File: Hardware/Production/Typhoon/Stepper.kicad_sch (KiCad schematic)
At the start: 14 parts, among them IC1 TMC2209-LA, J3 Motor Breakout

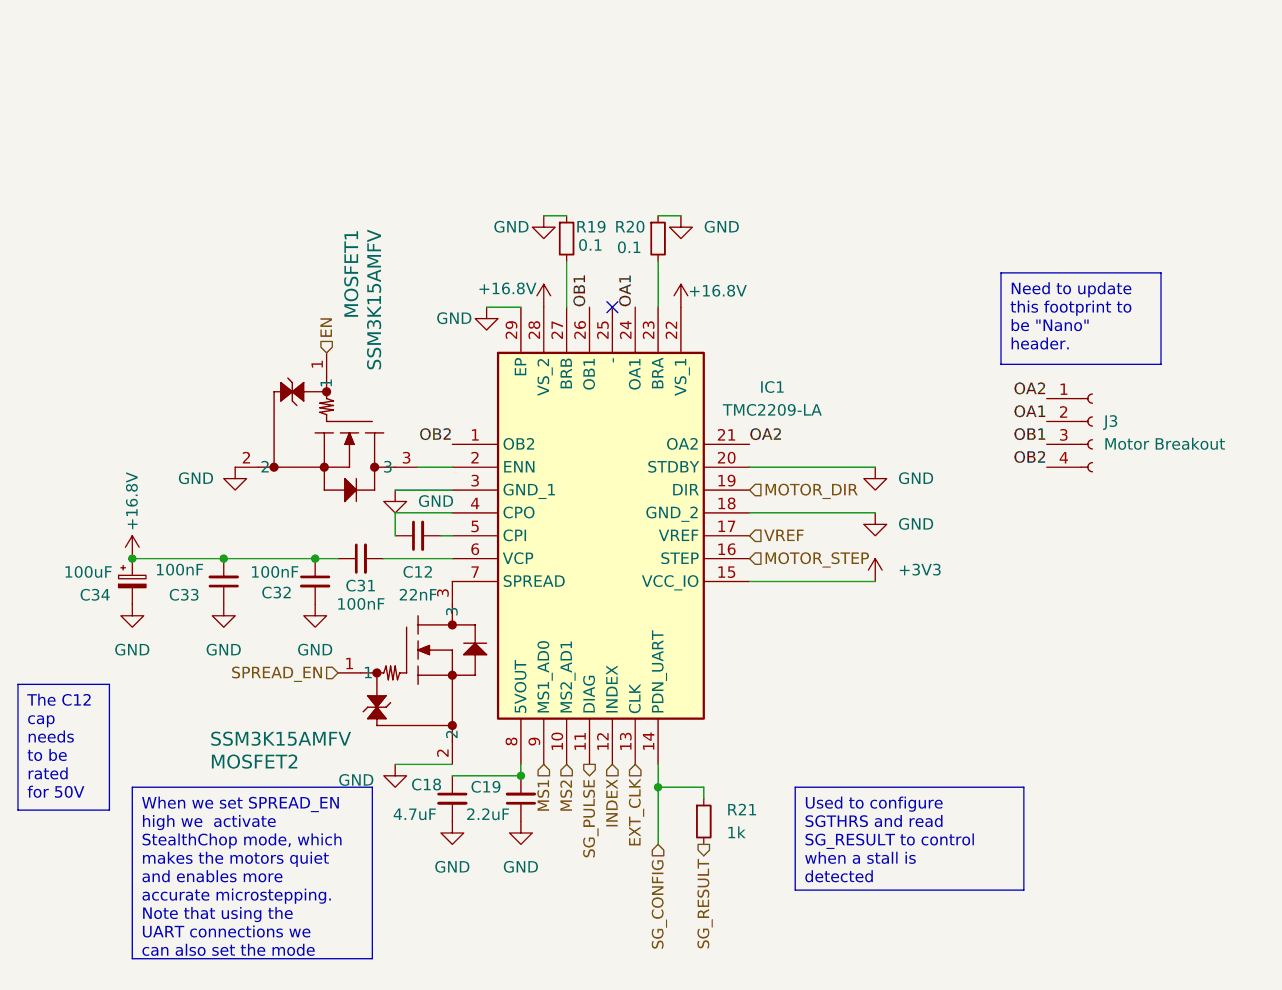
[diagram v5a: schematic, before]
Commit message: Small fixes to some footprints and used a different model for NMOS transistors
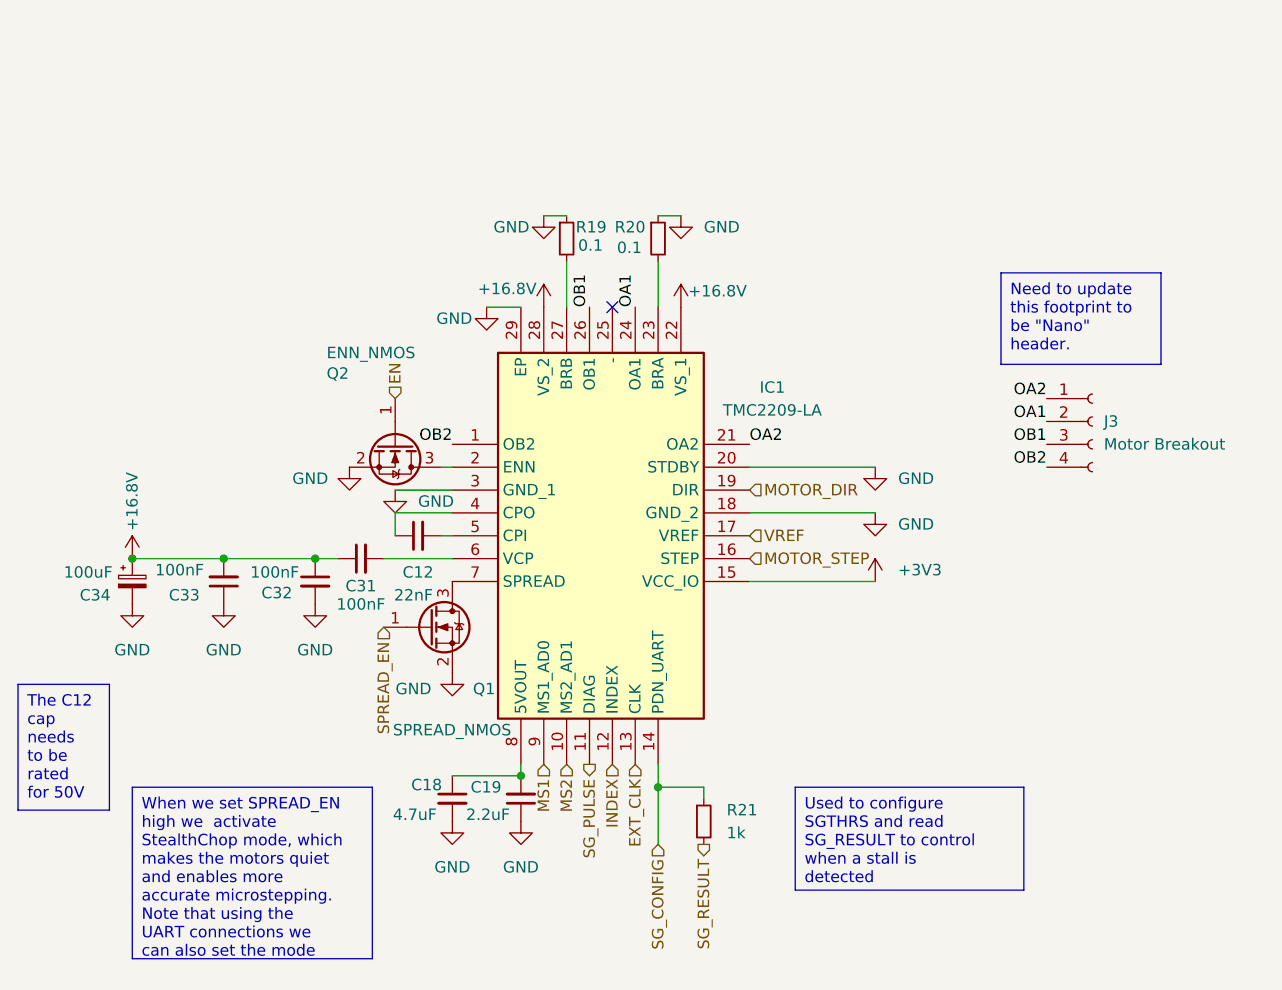
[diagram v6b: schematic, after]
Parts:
- removed MOSFET1, MOSFET2: SSM3K15AMFV, VESM_TOS, symbol SSM3K15AMFV:SSM3K15AMFV
- added Q1: SPREAD_NMOS, iclr:SOT-723, symbol Device:Q_NMOS_GSD
- added Q2: ENN_NMOS, iclr:SOT-723, symbol Device:Q_NMOS_GSD
- J3: footprint Connector_Molex:Molex_Nano-Fit_105313-xx04_1x04_P2.50mm_Horizontal -> iclr:Molex_Nano-Fit_105313-xx04_1x04_P2.50mm_Horizontal
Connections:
- net EN: now also Q2.1 (G)
- net GND: now also Q1.2 (S), Q2.2 (S)
- net SPREAD_EN: now also Q1.1 (G)
- net at IC1.7 (SPREAD): now also Q1.3 (D)
- net at IC1.2 (ENN): now also Q2.3 (D)
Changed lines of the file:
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@@
 	(wire
 		(pts
-			(xy 106.68 133.35) (xy 100.33 133.35)
+			(xy 134.62 135.89) (xy 134.62 137.16)
 		)
 		(stroke
@@
 	(wire
 		(pts
-			(xy 134.62 135.89) (xy 134.62 137.16)
+			(xy 106.68 134.62) (xy 114.3 134.62)
 		)
 		(stroke
@@
 	(wire
 		(pts
-			(xy 106.68 134.62) (xy 114.3 134.62)
-		)
-		(stroke
-			(width 0)
-			(type default)
-		)
-	)
-	(wire
-		(pts
-			(xy 102.87 100.33) (xy 106.68 100.33)
+			(xy 105.41 100.33) (xy 106.68 100.33)
 		)
 		(stroke
@@
 	(hierarchical_label "EN"
 		(shape input)
-		(at 92.71 87.63 90)
+		(at 100.33 92.71 90)
 		(fields_autoplaced yes)
 		(effects
@@
 	(hierarchical_label "SPREAD_EN"
 		(shape input)
-		(at 93.98 123.19 180)
+		(at 99.06 118.11 270)
 		(fields_autoplaced yes)
 		(effects
@@
 	(symbol
 		(lib_id "power:GND")
-		(at 100.33 133.35 0)
+		(at 106.68 123.19 0)
 		(unit 1)
 		(exclude_from_sim no)
@@
 		(dnp no)
 		(property "Reference" "#PWR068"
-			(at 100.33 139.7 0)
+			(at 106.68 129.54 0)
 			(effects
 				(font
@@
 		)
 		(property "Value" "GND"
-			(at 96.012 135.128 0)
+			(at 102.362 124.968 0)
 			(effects
 				(font
@@
 		)
 		(property "Footprint" ""
-			(at 100.33 133.35 0)
+			(at 106.68 123.19 0)
 			(effects
 				(font
@@
 		)
 		(property "Datasheet" ""
-			(at 100.33 133.35 0)
+			(at 106.68 123.19 0)
 			(effects
 				(font
@@
 		)
 		(property "Description" "Power symbol creates a global label with name \"GND\" , ground"
-			(at 100.33 133.35 0)
+			(at 106.68 123.19 0)
 			(effects
 				(font
@@
 				(path "/7db990e4-92e1-4f99-b4d2-435bbec1ba83/8de86a23-669c-43a7-bbab-df851b7a13ef"
 					(reference "C18")
+					(unit 1)
+				)
+			)
+		)
+	)
+	(symbol
+		(lib_id "Device:Q_NMOS_GSD")
+		(at 100.33 97.79 270)
+		(unit 1)
+		(exclude_from_sim no)
+		(in_bom yes)
+		(on_board yes)
+		(dnp no)
+		(property "Reference" "Q2"
+			(at 92.71 89.916 90)
+			(effects
+				(font
+					(size 1.27 1.27)
+				)
+				(justify left)
+			)
+		)
+		(property "Value" "ENN_NMOS"
+			(at 92.71 87.63 90)
+			(effects
+				(font
+					(size 1.27 1.27)
+				)
+				(justify left)
+			)
+		)
+		(property "Footprint" "iclr:SOT-723"
+			(at 102.87 102.87 0)
+			(effects
+				(font
+					(size 1.27 1.27)
+				)
+				(hide yes)
+			)
+		)
+		(property "Datasheet" "~"
+			(at 100.33 97.79 0)
+			(effects
+				(font
+					(size 1.27 1.27)
+				)
+				(hide yes)
+			)
+		)
+		(property "Description" "N-MOSFET transistor, gate/source/drain"
+			(at 100.33 97.79 0)
+			(effects
+				(font
+					(size 1.27 1.27)
+				)
+				(hide yes)
+			)
+		)
+		(pin "2"
+		)
+		(pin "3"
+		)
+		(pin "1"
+		)
+		(instances
+			(project "Typhoon"
+				(path "/7db990e4-92e1-4f99-b4d2-435bbec1ba83/8de86a23-669c-43a7-bbab-df851b7a13ef"
+					(reference "Q2")
 					(unit 1)
 				)
@@
 		(lib_name "GND_2")
 		(lib_id "power:GND")
-		(at 82.55 100.33 0)
+		(at 95.25 100.33 0)
 		(unit 1)
 		(exclude_from_sim no)
@@
 		(dnp no)
 		(property "Reference" "#PWR016"
-			(at 82.55 106.68 0)
+			(at 95.25 106.68 0)
 			(effects
 				(font
@@
 		)
 		(property "Value" "GND"
-			(at 76.2 101.6 0)
+			(at 88.9 101.6 0)
 			(effects
 				(font
@@
 		)
 		(property "Footprint" ""
-			(at 82.55 100.33 0)
+			(at 95.25 100.33 0)
 			(effects
 				(font
@@
 		)
 		(property "Datasheet" ""
-			(at 82.55 100.33 0)
+			(at 95.25 100.33 0)
 			(effects
 				(font
@@
 		)
 		(property "Description" "Power symbol creates a global label with name \"GND\" , ground"
-			(at 82.55 100.33 0)
+			(at 95.25 100.33 0)
 			(effects
 				(font
@@
 	)
 	(symbol
-		(lib_id "SSM3K15AMFV:SSM3K15AMFV")
-		(at 96.52 115.57 0)
-		(unit 1)
-		(exclude_from_sim no)
-		(in_bom yes)
-		(on_board yes)
-		(dnp no)
-		(property "Reference" "MOSFET2"
-			(at 79.756 133.096 0)
-			(effects
-				(font
-					(size 1.524 1.524)
-				)
-				(justify left)
-			)
-		)
-		(property "Value" "SSM3K15AMFV"
-			(at 79.756 130.556 0)
-			(effects
-				(font
-					(size 1.524 1.524)
-				)
-				(justify left)
-			)
-		)
-		(property "Footprint" "VESM_TOS"
-			(at 96.52 115.57 0)
-			(effects
-				(font
-					(size 1.27 1.27)
-					(italic yes)
-				)
-				(hide yes)
-			)
-		)
-		(property "Datasheet" "SSM3K15AMFV"
-			(at 96.52 115.57 0)
-			(effects
-				(font
-					(size 1.27 1.27)
-					(italic yes)
-				)
-				(hide yes)
-			)
-		)
-		(property "Description" ""
-			(at 96.52 115.57 0)
-			(effects
-				(font
-					(size 1.27 1.27)
-				)
-				(hide yes)
-			)
-		)
-		(pin "2"
-		)
-		(pin "1"
-		)
-		(pin "3"
-		)
-		(instances
-			(project "Typhoon"
-				(path "/7db990e4-92e1-4f99-b4d2-435bbec1ba83/8de86a23-669c-43a7-bbab-df851b7a13ef"
-					(reference "MOSFET2")
-					(unit 1)
-				)
-			)
-		)
-	)
-	(symbol
 		(lib_id "Device:C_Polarized_Small")
 		(at 71.12 113.03 0)
@@
 			)
 		)
-		(property "Footprint" "Connector_Molex:Molex_Nano-Fit_105313-xx04_1x04_P2.50mm_Horizontal"
+		(property "Footprint" "iclr:Molex_Nano-Fit_105313-xx04_1x04_P2.50mm_Horizontal"
 			(at 177.8 95.25 0)
 			(effects
@@
 		)
 		(property "Value" "22nF"
-			(at 102.87 114.554 90)
+			(at 102.362 114.554 90)
 			(effects
 				(font
@@
 	)
 	(symbol
-		(lib_id "SSM3K15AMFV:SSM3K15AMFV")
-		(at 100.33 90.17 270)
-		(unit 1)
-		(exclude_from_sim no)
-		(in_bom yes)
-		(on_board yes)
-		(dnp no)
-		(property "Reference" "MOSFET1"
-			(at 95.504 73.914 0)
-			(effects
-				(font
-					(size 1.524 1.524)
+		(lib_id "Device:Q_NMOS_GSD")
+		(at 104.14 118.11 0)
+		(unit 1)
+		(exclude_from_sim no)
+		(in_bom yes)
+		(on_board yes)
+		(dnp no)
+		(property "Reference" "Q1"
+			(at 108.966 124.968 0)
+			(effects
+				(font
+					(size 1.27 1.27)
 				)
 				(justify left)
 			)
 		)
-		(property "Value" "SSM3K15AMFV"
-			(at 98.044 73.914 0)
-			(effects
-				(font
-					(size 1.524 1.524)
+		(property "Value" "SPREAD_NMOS"
+			(at 100.076 129.54 0)
+			(effects
+				(font
+					(size 1.27 1.27)
 				)
 				(justify left)
 			)
 		)
-		(property "Footprint" "VESM_TOS"
-			(at 100.33 90.17 0)
-			(effects
-				(font
-					(size 1.27 1.27)
-					(italic yes)
-				)
-				(hide yes)
-			)
-		)
-		(property "Datasheet" "SSM3K15AMFV"
-			(at 100.33 90.17 0)
-			(effects
-				(font
-					(size 1.27 1.27)
-					(italic yes)
-				)
-				(hide yes)
-			)
-		)
-		(property "Description" ""
-			(at 100.33 90.17 0)
+		(property "Footprint" "iclr:SOT-723"
+			(at 109.22 115.57 0)
+			(effects
+				(font
+					(size 1.27 1.27)
+				)
+				(hide yes)
+			)
+		)
+		(property "Datasheet" "~"
+			(at 104.14 118.11 0)
+			(effects
+				(font
+					(size 1.27 1.27)
+				)
+				(hide yes)
+			)
+		)
+		(property "Description" "N-MOSFET transistor, gate/source/drain"
+			(at 104.14 118.11 0)
 			(effects
 				(font
@@
 		(pin "2"
 		)
-		(pin "1"
-		)
 		(pin "3"
 		)
+		(pin "1"
+		)
 		(instances
 			(project ""
 				(path "/7db990e4-92e1-4f99-b4d2-435bbec1ba83/8de86a23-669c-43a7-bbab-df851b7a13ef"
-					(reference "MOSFET1")
-					(unit 1)
-				)
+					(reference "Q1")
+					(unit 1)
+				)
